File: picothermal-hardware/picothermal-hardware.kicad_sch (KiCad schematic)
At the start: 73 parts, among them J1 TC2030-CTX, J2 USB-C Plug, SW1 SW_Push, SW2 SW_Push, U1 W25Q16JV, U4 RP2040, U7 Flir LEPTON, Y1 ECS-2520MV-250-CL, Y2 12MHz

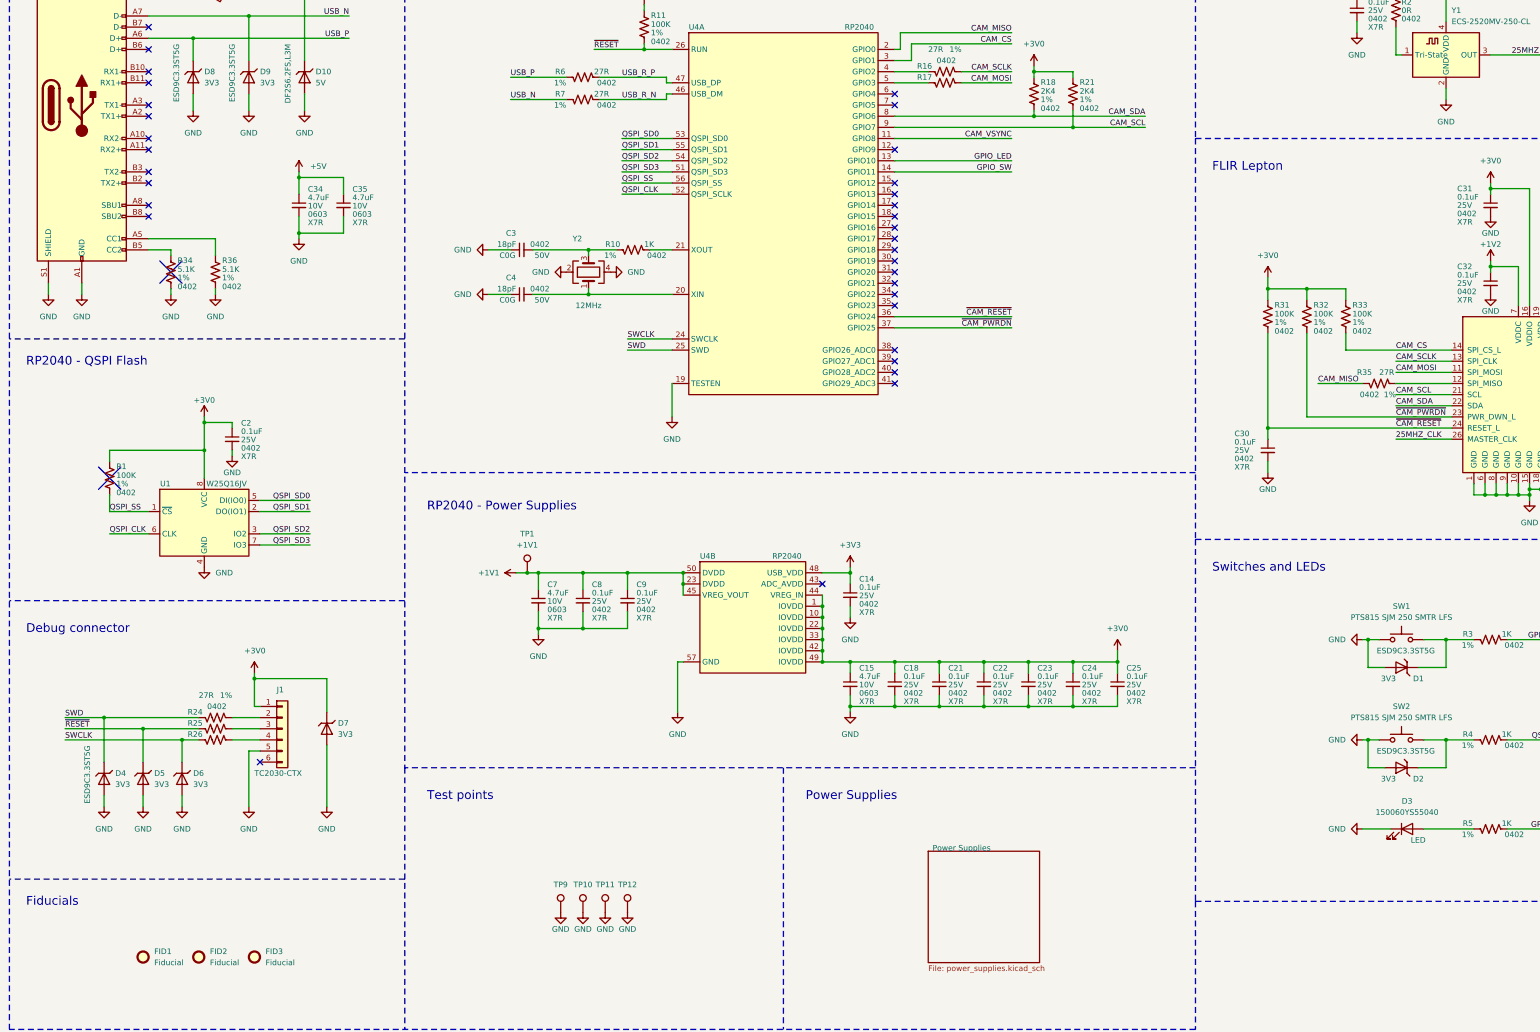
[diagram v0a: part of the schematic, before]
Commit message: Updated hardware project to work with Kicad 7.0
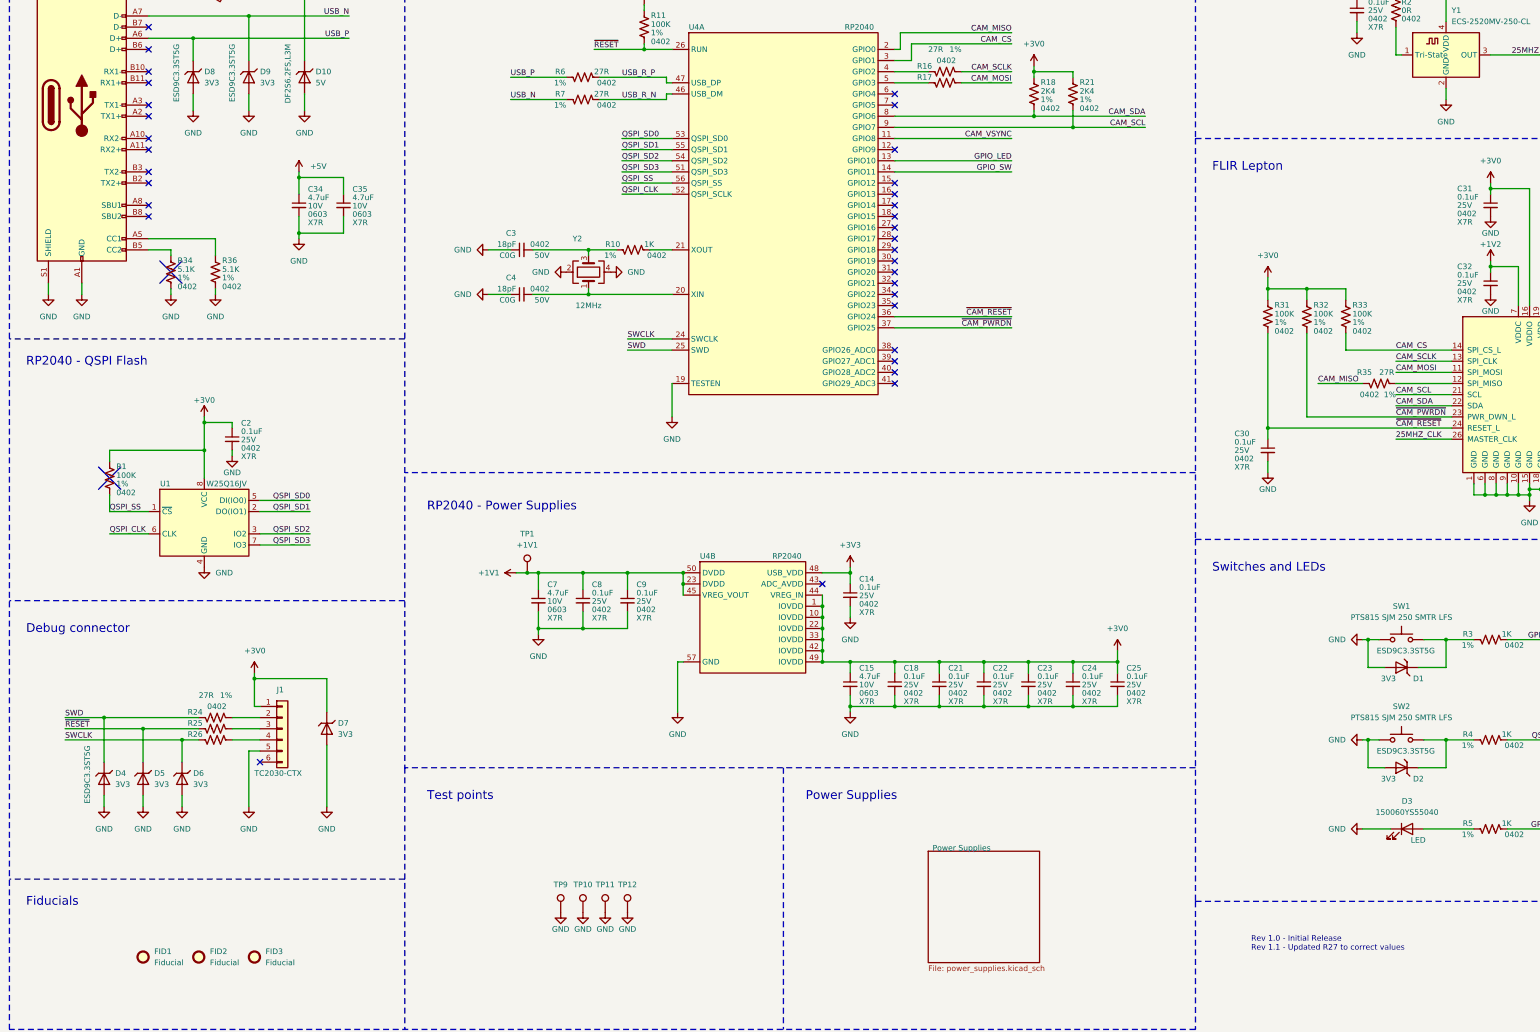
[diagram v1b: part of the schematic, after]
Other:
- note added: "Rev 1.0 - Initial Release Rev 1.1 - Updated R27 to correct values"
